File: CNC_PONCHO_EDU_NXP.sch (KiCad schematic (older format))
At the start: 0 parts

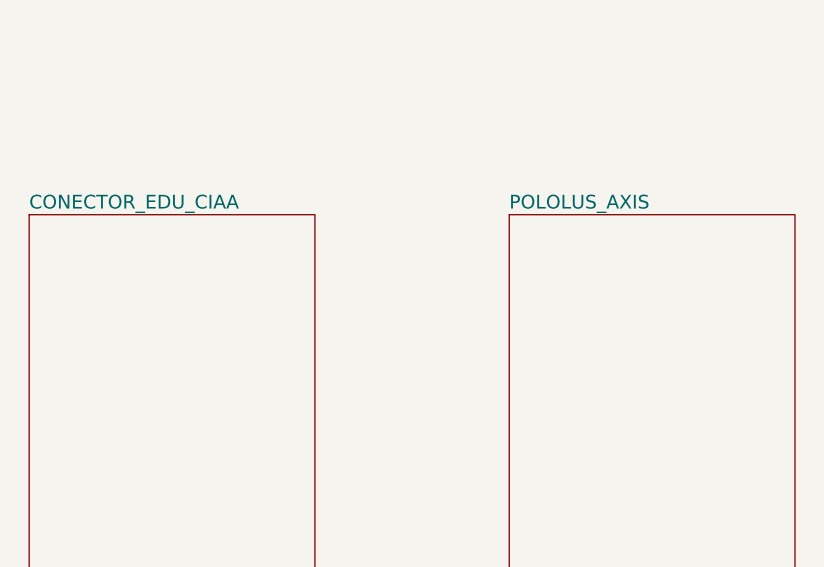
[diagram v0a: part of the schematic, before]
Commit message: Adicion de documentacion
Creacion y adicion de componente A4988 en hoja POLOLUS_AXIS.sch, Avance parcialmente completo de  hoja POLOLUS_AXIS.sch
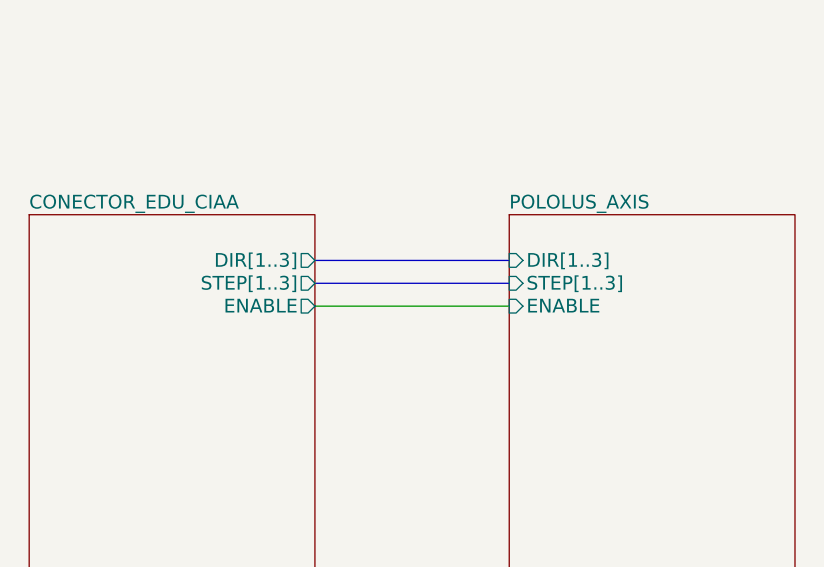
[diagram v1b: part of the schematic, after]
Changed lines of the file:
@@
 LIBS:Poncho_Esqueleto
 LIBS:Misc_Poncho_Grande
+LIBS:CNC_PONCHO_EDU_NXP-cache
 EELAYER 25 0
 EELAYER END
@@
 F0 "CONECTOR_EDU_CIAA" 60
 F1 "CONECTOR_EDU_CIAA.sch" 60
-$EndSheet
-$Sheet
-S 5400 3250 1250 2500
-U 583A30FC
-F0 "POLOLUS_AXIS" 60
-F1 "POLOLUS_AXIS.sch" 60
+F2 "DIR[1..3]" O R 4550 3450 60
+F3 "STEP[1..3]" O R 4550 3550 60
+F4 "ENABLE" O R 4550 3650 60
 $EndSheet
 $Sheet
@@
 Text Notes 1100 1200 0    197  ~ 39
 Poncho CNC
+$Sheet
+S 5400 3250 1250 2500
+U 583A30FC
+F0 "POLOLUS_AXIS" 60
+F1 "POLOLUS_AXIS.sch" 60
+F2 "DIR[1..3]" I L 5400 3450 60
+F3 "STEP[1..3]" I L 5400 3550 60
+F4 "ENABLE" I L 5400 3650 60
+$EndSheet
+Wire Bus Line
+	4550 3450 5400 3450
+Wire Bus Line
+	4550 3550 5400 3550
+Wire Wire Line
+	4550 3650 5400 3650
 $EndSCHEMATC

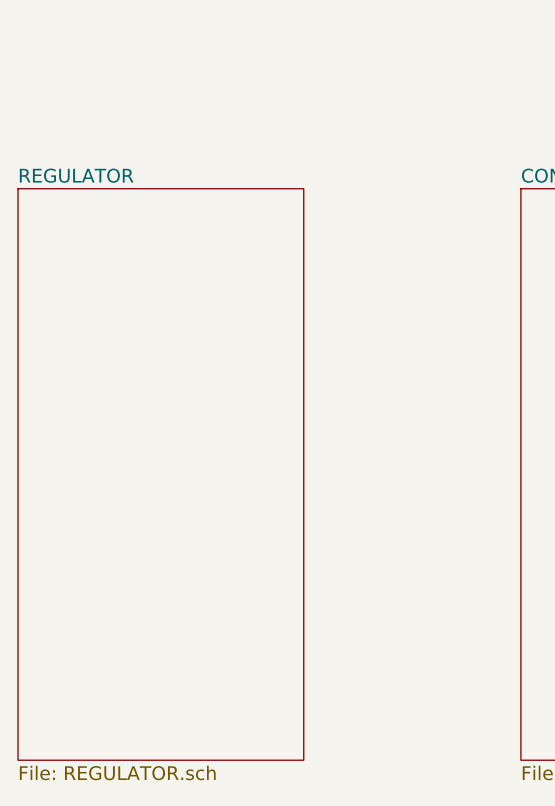
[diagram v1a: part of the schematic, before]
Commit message: Reorganizacion de carpetas y avance de esquematico
Creacion de componente LM2596. Hoja REGULADOR finalizada. Avance parcial en hoja CONECTOR_EDU_CIAA. Creacion de carpetas datasheet y doc. Adicion de hojas de datos de LM2596, A4988, MMBT2222A. Adicion de documentacion LICENCIA, README, Revisiones.
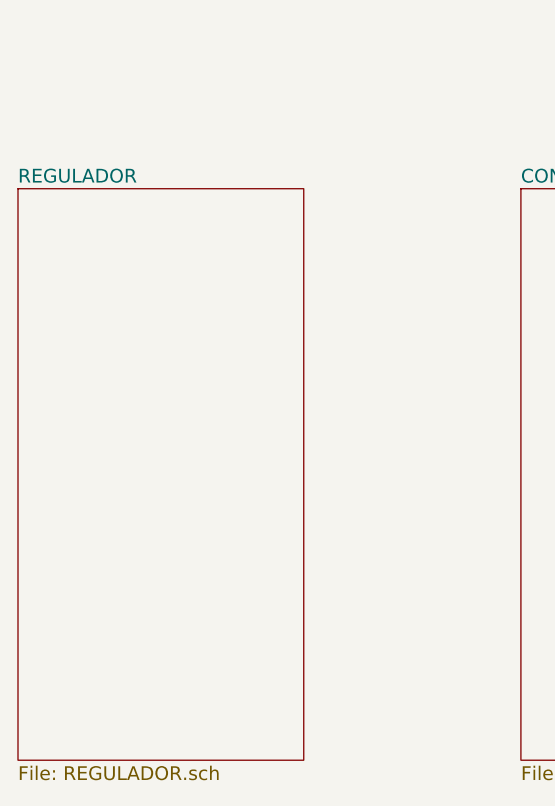
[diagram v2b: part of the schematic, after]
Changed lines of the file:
@@
 Comp "CESE - Curso de diseño de PCB"
 Comment1 "Autor: Marcelo Franz Moreno Marin"
-Comment2 "Licencia:"
+Comment2 "Licencia: doc/LICENCIA"
 Comment3 ""
 Comment4 ""
@@
 S 1100 3250 1250 2500
 U 583A30FF
-F0 "REGULATOR" 60
-F1 "REGULATOR.sch" 60
+F0 "REGULADOR" 60
+F1 "REGULADOR.sch" 60
 $EndSheet
 Text Notes 1100 1200 0    197  ~ 39
